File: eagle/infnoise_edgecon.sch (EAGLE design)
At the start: 28 parts, among them SW1 MC74VHC1G66DFT1G, SW2 MC74VHC1G66DFT1G, X1 USB

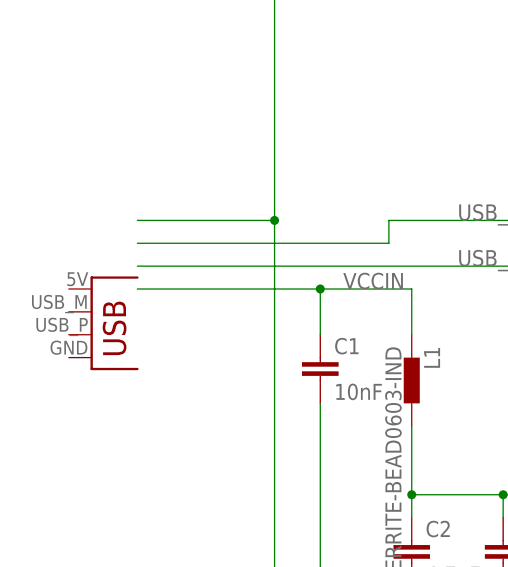
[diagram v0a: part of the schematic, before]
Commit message: Updated README to use modular noise multiplier
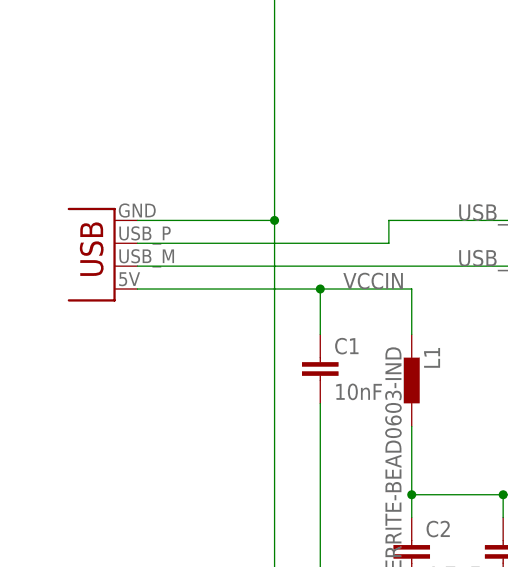
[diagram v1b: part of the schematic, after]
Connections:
- net GND: now also X1.GND
- net USB_M: now also X1.D-
- net USB_P: now also X1.D+
- net VCCIN: now also X1.VCC
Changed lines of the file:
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@@
 <instance part="FID2" gate="G$1" x="-17.78" y="83.82"/>
 <instance part="FID3" gate="G$1" x="-7.62" y="83.82"/>
-<instance part="X1" gate="G$1" x="-45.72" y="20.32"/>
+<instance part="X1" gate="G$1" x="-43.18" y="35.56" rot="R180"/>
 </instances>
 <busses>
@@
 <wire x1="-12.7" y1="35.56" x2="-12.7" y2="33.02" width="0.1524" layer="91"/>
 <wire x1="-12.7" y1="33.02" x2="-40.64" y2="33.02" width="0.1524" layer="91"/>
+<pinref part="X1" gate="G$1" pin="D+"/>
 </segment>
 </net>
@@
 <label x="-5.08" y="30.48" size="1.778" layer="95"/>
 <junction x="15.24" y="30.48"/>
+<pinref part="X1" gate="G$1" pin="D-"/>
 </segment>
 </net>
@@
 <wire x1="-40.64" y1="27.94" x2="-20.32" y2="27.94" width="0.1524" layer="91"/>
 <junction x="-20.32" y="27.94"/>
+<pinref part="X1" gate="G$1" pin="VCC"/>
 </segment>
 </net>
@@
 <wire x1="132.08" y1="5.08" x2="132.08" y2="-15.24" width="0.1524" layer="91"/>
 <junction x="132.08" y="-15.24"/>
+<pinref part="X1" gate="G$1" pin="GND"/>
 </segment>
 </net>
